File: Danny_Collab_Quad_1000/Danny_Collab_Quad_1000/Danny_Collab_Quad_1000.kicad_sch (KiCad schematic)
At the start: 3 parts

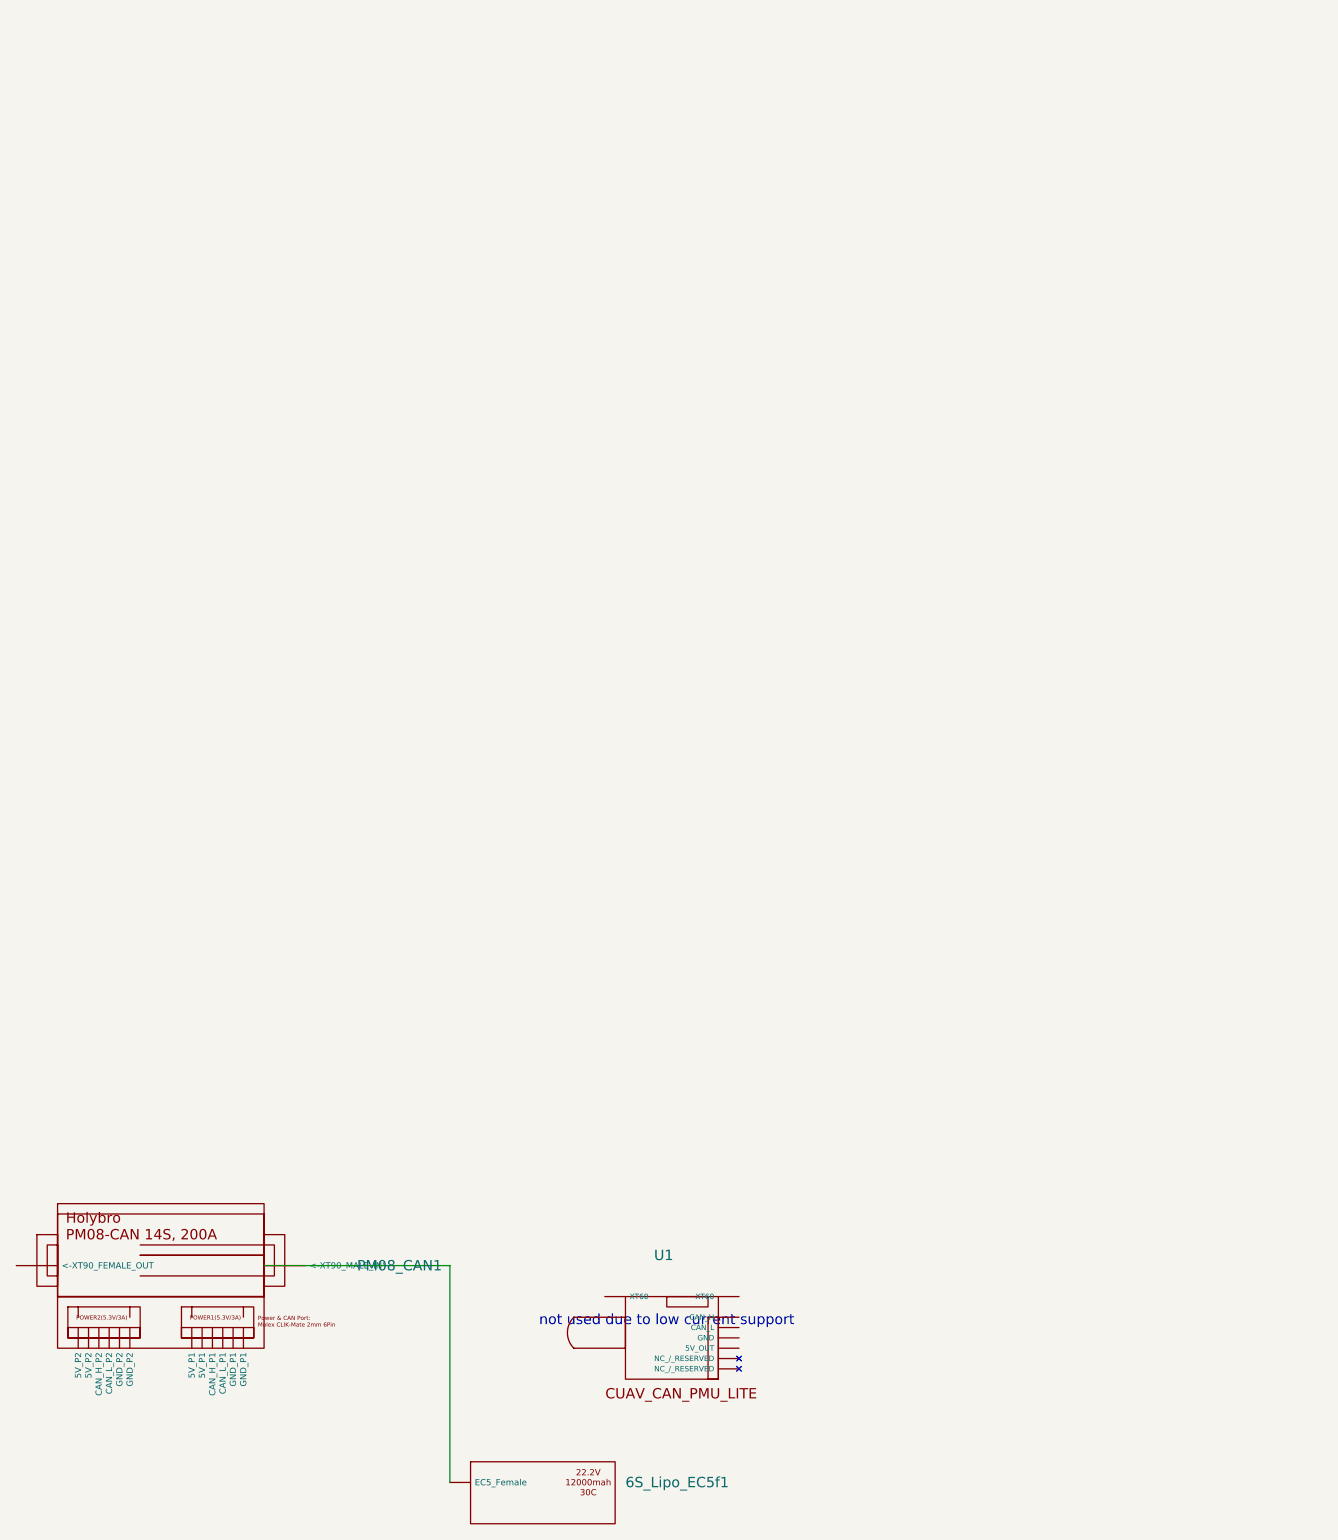
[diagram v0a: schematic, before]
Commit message: KiCad: add backups and update project/schematic
Add project backup archives and fp-info-cache, remove transient autosave/.lck files. Update Danny_Collab_Quad_1000.kicad_prl (net inspector column settings) and expand Danny_Collab_Quad_1000.kicad_pro with board design defaults, DRC rule severities, rules, teardrop and tuning settings. Large schematic addition: embed CUAV_Pixhawk_V6X symbol into Danny_Collab_Quad_1000.kicad_sch. Also add a Model A backup for KicadTest_forRTKBASE and remove its autosave/lock artifacts.
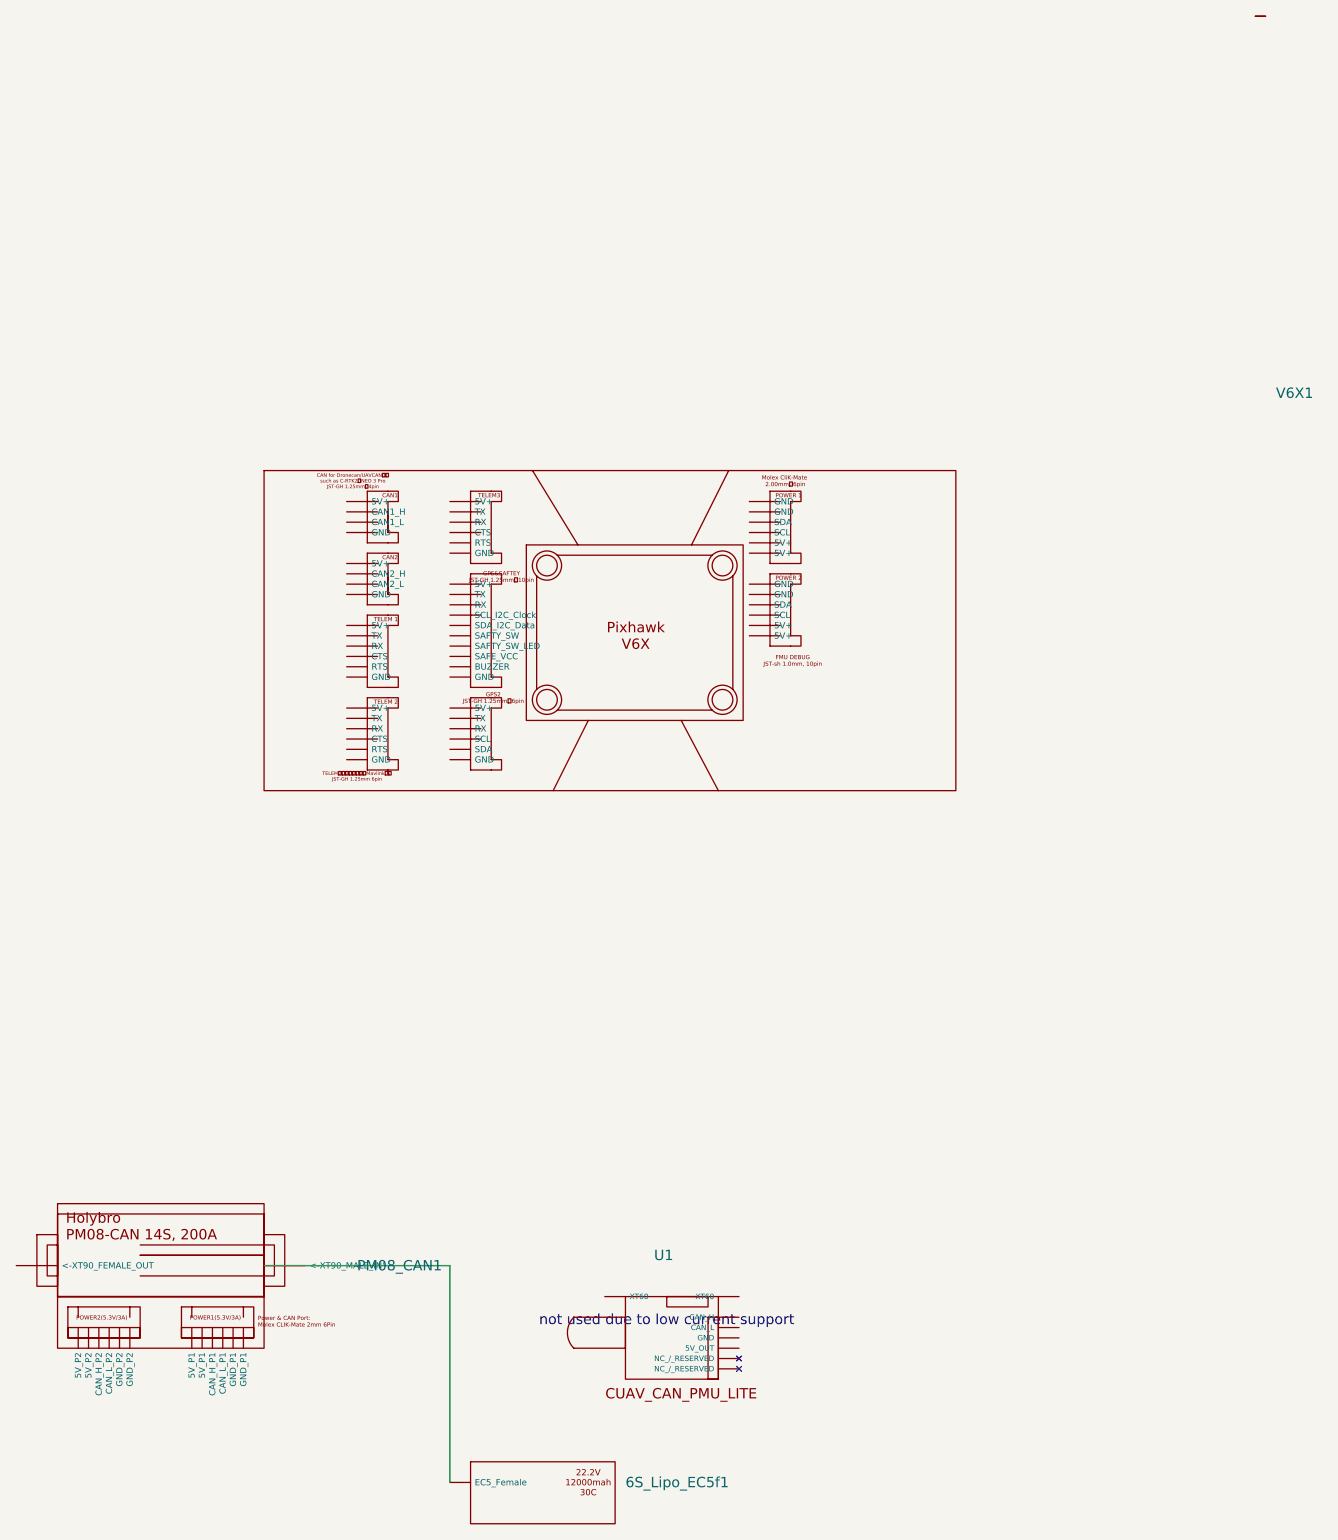
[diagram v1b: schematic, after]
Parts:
- added V6X1: ~, symbol Drones:CUAV_Pixhawk_V6X
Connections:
- net at PM08_CAN1. (<-XT90_MALE_IN'): now also 6S_Lipo_EC5f1. (EC5_Female)
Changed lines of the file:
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@@
+		)
+	)
+	(symbol
+		(lib_id "Drones:CUAV_Pixhawk_V6X")
+		(at 128.27 92.71 0)
+		(unit 1)
+		(exclude_from_sim no)
+		(in_bom yes)
+		(on_board yes)
+		(dnp no)
+		(fields_autoplaced yes)
+		(property "Reference" "V6X1"
+			(at 236.22 55.2449 0)
+			(effects
+				(font
+					(size 1.27 1.27)
+				)
+				(justify left)
+			)
+		)
+		(property "Value" "~"
+			(at 236.22 57.7849 0)
+			(effects
+				(font
+					(size 1.27 1.27)
+				)
+				(justify left)
+			)
+		)
+		(property "Footprint" ""
+			(at 128.27 92.71 0)
+			(effects
+				(font
+					(size 1.27 1.27)
+				)
+				(hide yes)
+			)
+		)
+		(property "Datasheet" ""
+			(at 128.27 92.71 0)
+			(effects
+				(font
+					(size 1.27 1.27)
+				)
+				(hide yes)
+			)
+		)
+		(property "Description" ""
+			(at 128.27 92.71 0)
+			(effects
+				(font
+					(size 1.27 1.27)
+				)
+				(hide yes)
+			)
+		)
+		(pin ""
+		)
+		(pin ""
+		)
+		(pin ""
+		)
+		(pin ""
+		)
+		(pin ""
+		)
+		(pin ""
+		)
+		(pin ""
+		)
+		(pin ""
+		)
+		(pin ""
+		)
+		(pin ""
+		)
+		(pin ""
+		)
+		(pin ""
+		)
+		(pin ""
+		)
+		(pin ""
+		)
+		(pin ""
+		)
+		(pin ""
+		)
+		(pin ""
+		)
+		(pin ""
+		)
+		(pin ""
+		)
+		(pin ""
+		)
+		(pin ""
+		)
+		(pin ""
+		)
+		(pin ""
+		)
+		(pin ""
+		)
+		(pin ""
+		)
+		(pin ""
+		)
+		(pin ""
+		)
+		(pin ""
+		)
+		(pin ""
+		)
+		(pin ""
+		)
+		(pin ""
+		)
+		(pin ""
+		)
+		(pin ""
+		)
+		(pin ""
+		)
+		(pin ""
+		)
+		(pin ""
+		)
+		(pin ""
+		)
+		(pin ""
+		)
+		(pin ""
+		)
+		(pin ""
+		)
+		(pin ""
+		)
+		(pin ""
+		)
+		(pin ""
+		)
+		(pin ""
+		)
+		(pin ""
+		)
+		(pin ""
+		)
+		(pin ""
+		)
+		(pin ""
+		)
+		(pin ""
+		)
+		(pin ""
+		)
+		(pin ""
+		)
+		(pin ""
+		)
+		(pin ""
+		)
+		(pin ""
+		)
+		(instances
+			(project ""
+				(path "/35238ef7-ffdb-4f16-8db9-6f0c236a0719"
+					(reference "V6X1")
+					(unit 1)
+				)
+			)
 		)
 	)
